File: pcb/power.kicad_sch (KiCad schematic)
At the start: 11 parts, among them U1 MIC5335-JGYMT, U2 NCP163AFCT180T2G

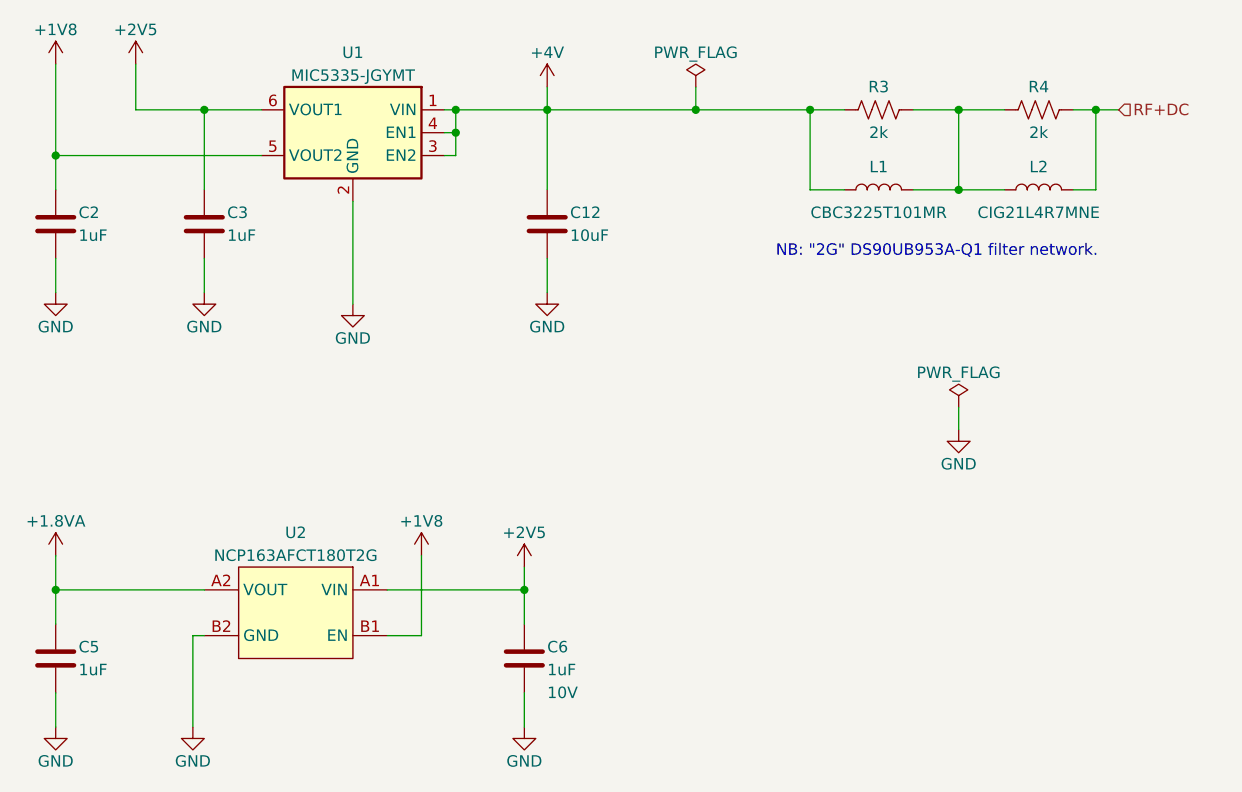
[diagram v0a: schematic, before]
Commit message: Inital routing complete
- Addressed Aaron's review
- Pullup on output side of analog switch to prevent floating SDA
- Other minor changes
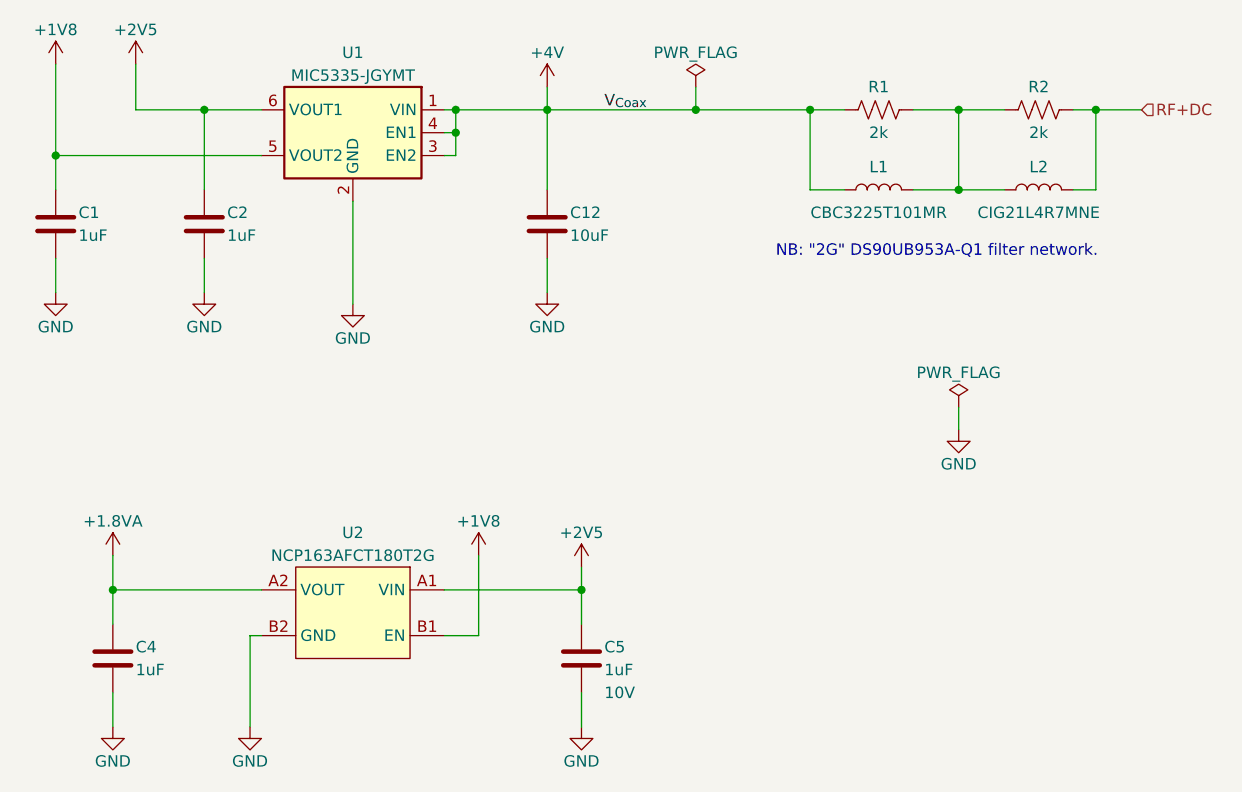
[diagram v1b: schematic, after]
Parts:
- renumbered C2 to C1, C3 to C2, C5 to C4, C6 to C5, R3 to R1, R4 to R2
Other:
- moved on the sheet: C4, C5, U2

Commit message: Address team comments
- Add extra mouse-bite supports
- Enbiggen cable strain relief spear
- Add DNP 0.1" header for bench debug
- Small routing changes
- Update and complete BOM
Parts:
- C1, C2, C4, C5: CASE/PACKAGE (none) -> 0201
- C12: CASE/PACKAGE (none) -> 0402
- L1: CASE/PACKAGE (none) -> 1210
- L2: CASE/PACKAGE (none) -> 0805
- R1, R2: CASE/PACKAGE (none) -> 0201; Tolerance (none) -> 1%

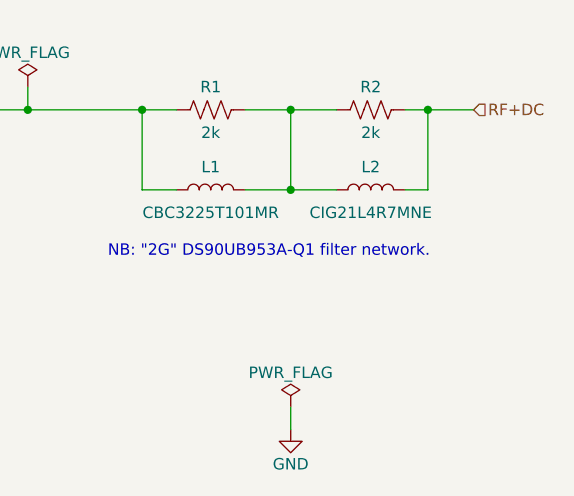
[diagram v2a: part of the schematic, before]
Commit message: Updates to design after feedback from assembler
- Replace obsolete TE_2013496-9 ZIF connector used by IMEC with
046844727002846+, which should fit NP 2.0 flex connectors (see design
folder for comparison). We will see.
- Replaced programmable MEMS oscillator with standard quartz since this
is a common frequency.
- Other BOM updates to account for obsolete or out of stock components
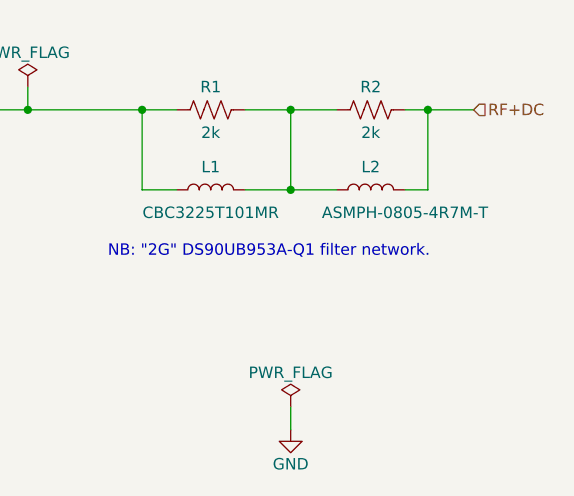
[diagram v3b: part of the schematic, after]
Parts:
- L2: value CIG21L4R7MNE -> ASMPH-0805-4R7M-T
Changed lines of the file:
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@@
       (effects (font (size 1.27 1.27)))
     )
-    (property "Value" "CIG21L4R7MNE" (at 207.01 74.93 90)
+    (property "Value" "ASMPH-0805-4R7M-T" (at 210.82 74.93 90)
       (effects (font (size 1.27 1.27)))
     )
